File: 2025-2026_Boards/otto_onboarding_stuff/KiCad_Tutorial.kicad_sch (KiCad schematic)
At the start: 22 parts, among them J1 USB_B_Micro, J3 Conn_01x04_Pin, SW1 SW_SPDT, U1 STM32F103C8T6, U3 AMS1117-3.3, Y1 16MHz

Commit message: Worked on onboarding project
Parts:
- added D1: LED, symbol Device:LED
- added J2, J4: Conn_01x04_Pin, symbol Connector:Conn_01x04_Pin
- added R3, R4, R5: R, symbol Device:R
- C12, C13: value C -> 22u
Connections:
- net +3.3V: now also C13.1, U3.2 (VO), D1.2 (A), J2.1 (Pin_1), J4.1 (Pin_1), R4.1, R5.1
- net GND: now also J2.4 (Pin_4), J4.4 (Pin_4), R3.2
- net VBUS: now also C12.1, U3.3 (VI)
- net I2C2_STL: now reaches U1.21 (PB10)
- net I2C2_STL: now also J4.2 (Pin_2), R4.2
- net I2C2_STA: now reaches U1.22 (PB11)
- net I2C2_STA: now also J4.3 (Pin_3), R5.2
- net USART1_TX: now reaches U1.42 (PB6)
- net USART1_TX: now also J2.2 (Pin_2)
- net USART1_RX: now reaches U1.43 (PB7)
- net USART1_RX: now also J2.3 (Pin_3)
- new net PWR_LED_K: D1.1 (K), R3.1
- no-connect marks 2 -> 29
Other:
- moved on the sheet: C11, Y1

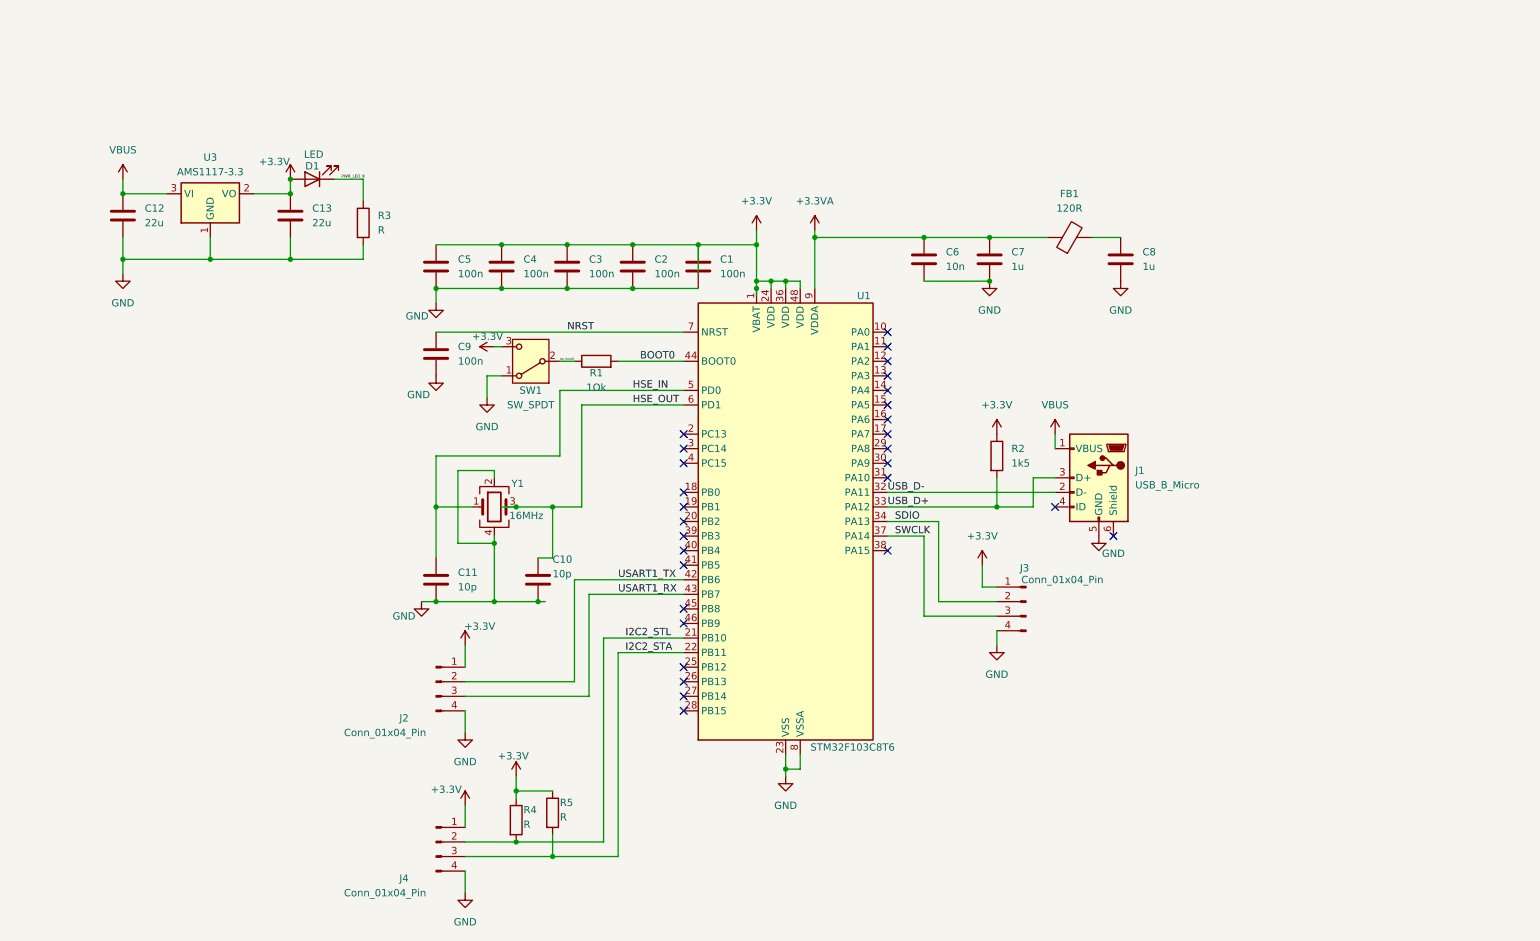
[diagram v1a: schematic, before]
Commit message: Finished KiCAD Schematic. Will start PCB Layout tomorrow.
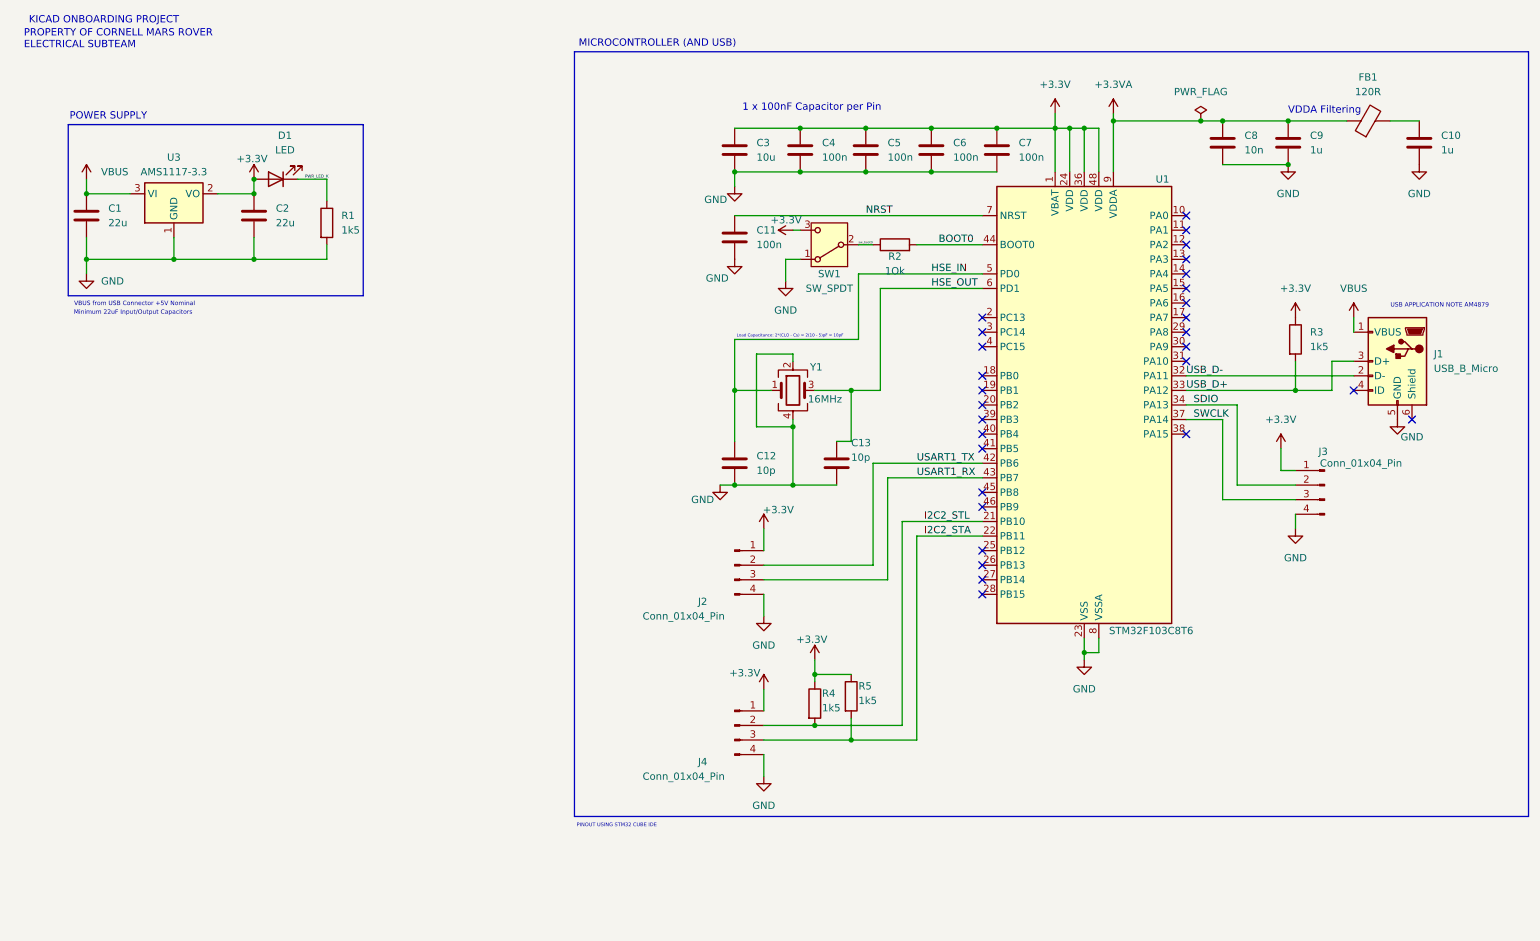
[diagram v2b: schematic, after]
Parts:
- C1: renamed from C12; footprint (none) -> Capacitor_SMD:C_0805_2012Metric
- C10: renamed from C8; footprint (none) -> Capacitor_SMD:C_0402_1005Metric
- C11: renamed from C9; footprint (none) -> Capacitor_SMD:C_0402_1005Metric
- C12: renamed from C11; footprint (none) -> Capacitor_SMD:C_0402_1005Metric
- C13: renamed from C10; footprint (none) -> Capacitor_SMD:C_0402_1005Metric
- C2: renamed from C13; footprint (none) -> Capacitor_SMD:C_0805_2012Metric
- C3: renamed from C5; value 100n -> 10u; footprint (none) -> Capacitor_SMD:C_0201_0603Metric
- C4: footprint (none) -> Capacitor_SMD:C_0402_1005Metric
- C5: renamed from C3; footprint (none) -> Capacitor_SMD:C_0402_1005Metric
- C6: renamed from C2; footprint (none) -> Capacitor_SMD:C_0402_1005Metric
- C7: renamed from C1; footprint (none) -> Capacitor_SMD:C_0402_1005Metric
- C8: renamed from C6; footprint (none) -> Capacitor_SMD:C_0402_1005Metric
- C9: renamed from C7; footprint (none) -> Capacitor_SMD:C_0402_1005Metric
- D1: footprint (none) -> Capacitor_SMD:C_0201_0603Metric
- FB1: footprint (none) -> LED_SMD:LED_0603_1608Metric
- J1: footprint (none) -> Connector_USB:USB_Micro-B_Wuerth_629105150521
- J2, J3, J4: footprint (none) -> Connector_PinHeader_2.54mm:PinHeader_1x04_P2.54mm_Vertical
- R1: renamed from R3; value R -> 1k5; footprint (none) -> Resistor_SMD:R_0402_1005Metric
- R2: renamed from R1; footprint (none) -> Resistor_SMD:R_0402_1005Metric
- R3: renamed from R2; footprint (none) -> Resistor_SMD:R_0402_1005Metric
- R4, R5: value R -> 1k5; footprint (none) -> Resistor_SMD:R_0402_1005Metric
- SW1: footprint (none) -> Button_Switch_THT:SW_Lever_1P2T_NKK_GW12LxH
- Y1: footprint (none) -> Crystal:Crystal_SMD_3225-4Pin_3.2x2.5mm
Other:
- note added: "1 x 100nF Capacitor per Pin"
- note added: "KICAD ONBOARDING PROJECT"
- note added: "Load Capacitance: 2*(CLO - Cs) = 2(10 - 5)pF = 10pF"
- note added: "MICROCONTROLLER (AND USB)"
- note added: "Minimum 22uF Input/Output Capacitors"
- note added: "PINOUT USING STM32 CUBE IDE"
- note added: "POWER SUPPLY"
- note added: "PROPERTY OF CORNELL MARS ROVER ELECTRICAL SUBTEAM"
- note added: "USB APPLICATION NOTE AM4879"
- note added: "VBUS from USB Connector +5V Nominal"
- note added: "VDDA Filtering"
- company: (none) -> CORNELL MARS ROVER ELECTRICAL SUBTEAM
- title: (none) -> ONBOARDING PROJECT
- moved on the sheet: C1, C10, C11, C12, C13, C2, C3, C4, C5, C6, C7, C8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

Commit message: Worked on wiring.
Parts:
- added H1, H2, H3, H4: MountingHole, MountingHole:MountingHole_2.2mm_M2, symbol Mechanical:MountingHole
- SW1: footprint Button_Switch_THT:SW_Lever_1P2T_NKK_GW12LxH -> Button_Switch_SMD:SW_SPDT_PCM12
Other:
- note added: "Mounting Holes"
- company: CORNELL MARS ROVER ELECTRICAL SUBTEAM -> CORNELL MARS ROVER
